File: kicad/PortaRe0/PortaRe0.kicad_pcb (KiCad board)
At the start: 6 copper layers, 135 x 77 mm, 357 parts, among them CN1 M.2, J1 Battery, J2 SPK_R, J3 SPK_L, J6 Fan, J9 PJ-307C, Q1 BSS138, SW1 SW_START, SW2 KillSW, U1 BQ25895RTWR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

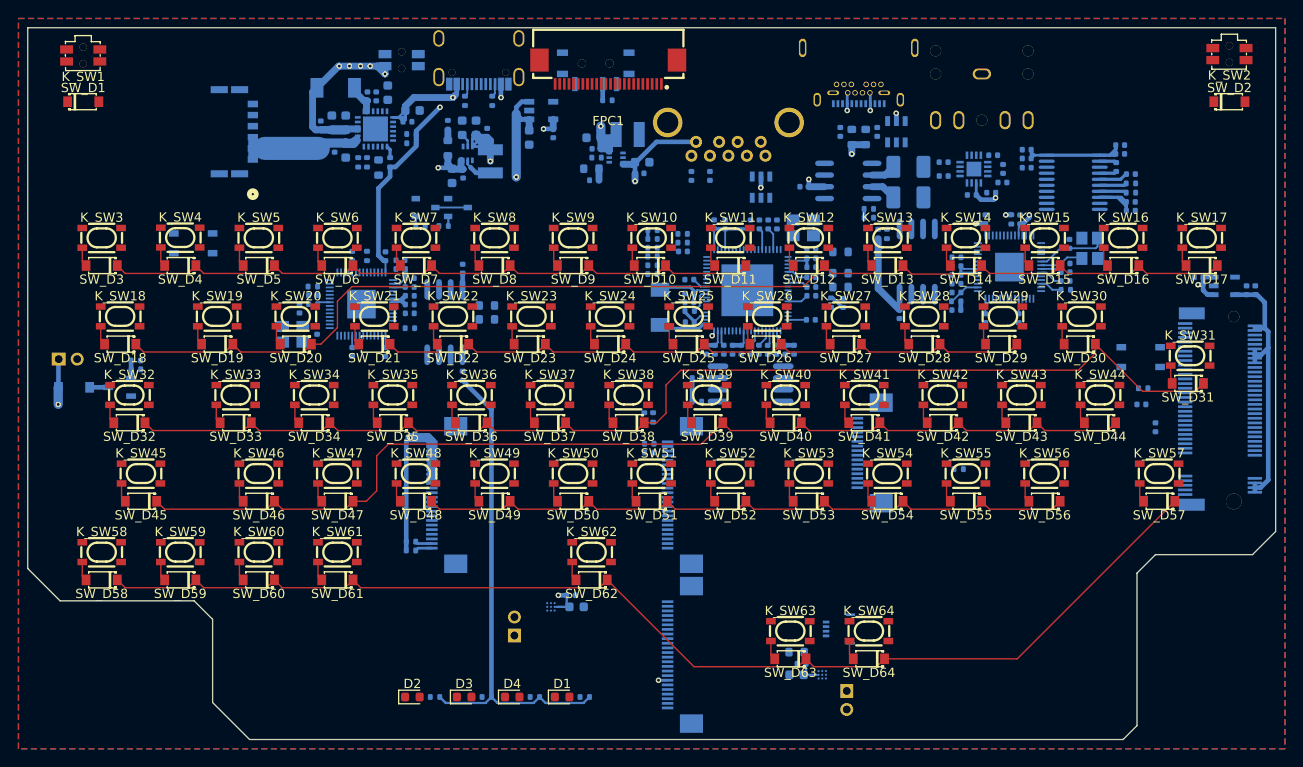
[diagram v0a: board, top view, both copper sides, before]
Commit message: Docs: session38終了処理・ルーティング大幅進捗（電源幹線〜USB差動ペア完了）
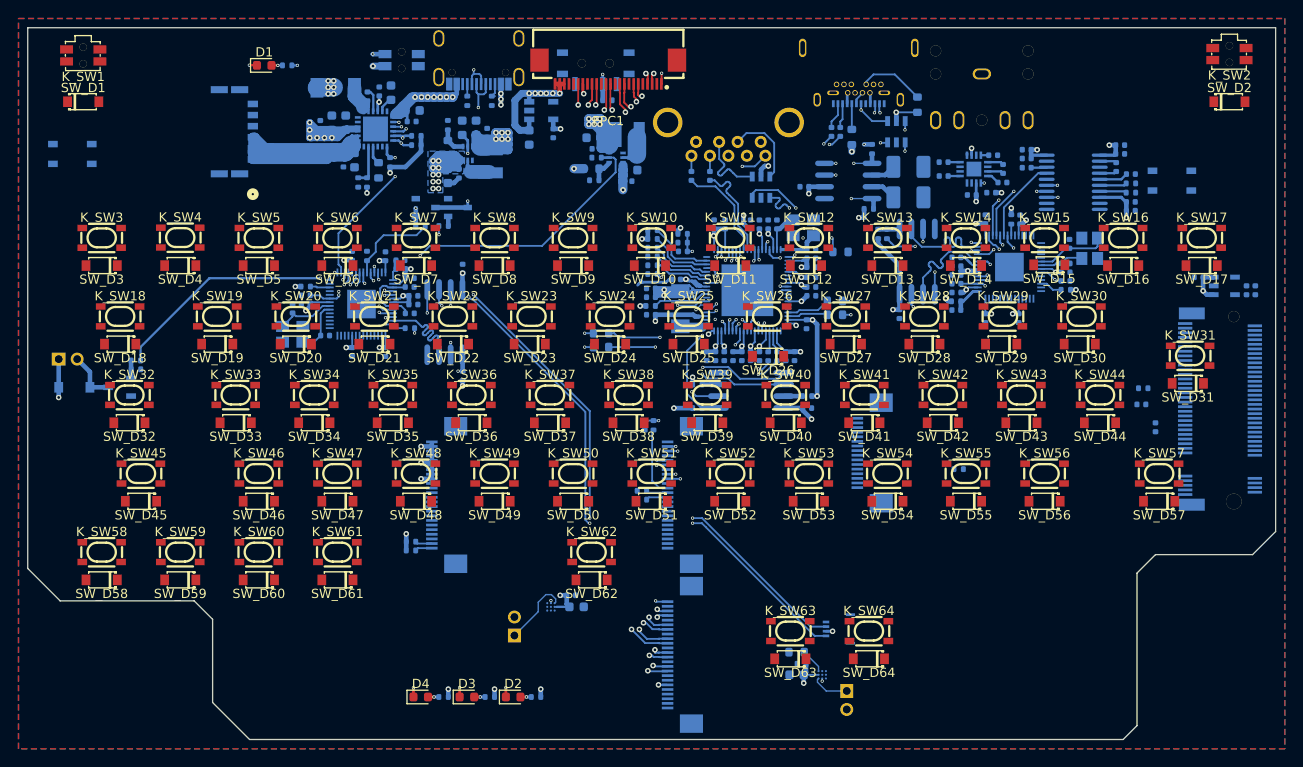
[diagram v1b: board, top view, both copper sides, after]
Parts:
- moved D1 75.5 mm to (175.6, 104.1)
- moved R3 75.5 mm to (178.1, 104.1)
- moved B_SW2 19.4 mm to (273.8, 116.5)
- moved B_SW1 16.3 mm to (154.8, 113.7)
- moved R27 12.7 mm to (212.0, 134.6), turned to 180 degrees
- moved R28 12.7 mm to (212.0, 133.1), turned to 180 degrees
- moved C66 12.0 mm to (234.3, 141.2), turned to 180 degrees
- moved R31 10.9 mm to (205.0, 172.4)
- moved D2 10.9 mm to (202.5, 172.4)
- moved R17 10.4 mm to (234.3, 139.8), turned to 180 degrees
- moved D4 9.90 mm to (192.5, 172.4)
- moved R33 9.87 mm to (195.0, 172.4)
- moved R25 7.43 mm to (241.3, 113.1), turned to -90 degrees
- moved R51 6.60 mm to (246.2, 108.3)
- moved R52 5.16 mm to (216.4, 151.1)
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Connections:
- FPC2 pad 18: 5V_SYS -> unconnected-(FPC2-Pad18)
- U8 pad B10: USB3_DP1_RX_N -> unconnected-(U8-SSRXn1-PadB10)
- U8 pad B11: USB3_DP1_RX_P -> unconnected-(U8-SSRXp1-PadB11)
- U8 pad B2: USB3_DP1_TX_P -> unconnected-(U8-SSTXp2-PadB2)
- U8 pad B3: USB3_DP1_TX_N -> unconnected-(U8-SSTXn2-PadB3)
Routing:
- net 5V_SYS: track 267.9 -> 119.8 mm, vias 8 -> 27
- net /keyboard/ROW7: track 129.2 -> 0.00 mm
- net /keyboard/ROW2: track 127.2 -> 0.00 mm
- net /keyboard/ROW4: track 127.1 -> 0.00 mm
- net /keyboard/ROW5: track 114.4 -> 0.00 mm
- net +3V3: track 165.1 -> 87.7 mm, vias 6 -> 34
- net 1V2_HUB: track 34.4 -> 111.8 mm, vias 0 -> 11
- net /keyboard/ROW6: track 73.6 -> 0.00 mm
- net /keyboard/ROW1: track 73.6 -> 0.00 mm
- net /keyboard/ROW3: track 73.4 -> 0.00 mm
- net STICK_X: track 0.00 -> 72.4 mm, vias 0 -> 4
- net STICK_Y: track 0.00 -> 72.0 mm, vias 0 -> 4
- net /Connectors/HDMI_CEC: track 0.00 -> 70.1 mm, vias 0 -> 2
- net /Connectors/HDMI_SDA: track 0.00 -> 69.3 mm, vias 0 -> 2
- net /Connectors/HDMI_SCL: track 0.00 -> 68.6 mm, vias 0 -> 2
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- added copper zone on In3.Cu, net +3V3
- added copper zone on In3.Cu, net /usb_hub/HUB_5V
- added copper zone on In3.Cu, net 3V3_HUB
- added copper zone on B.Cu, net 5V_SYS
- added copper zone on In3.Cu, net 5V_SYS
- added copper zone on In3.Cu, net VSYS
- removed copper zone on In3.Cu, net GND
